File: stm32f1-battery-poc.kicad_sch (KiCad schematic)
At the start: 0 parts

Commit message: schem: add STM32F103C8T6 symbol
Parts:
- added U1: STM32F103C8Tx, Package_QFP:LQFP-48_7x7mm_P0.5mm, symbol MCU_ST_STM32F1:STM32F103C8Tx
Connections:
- new net GND: U1.23 (VSS), U1.35 (VSS), U1.47 (VSS), U1.8 (VSSA)

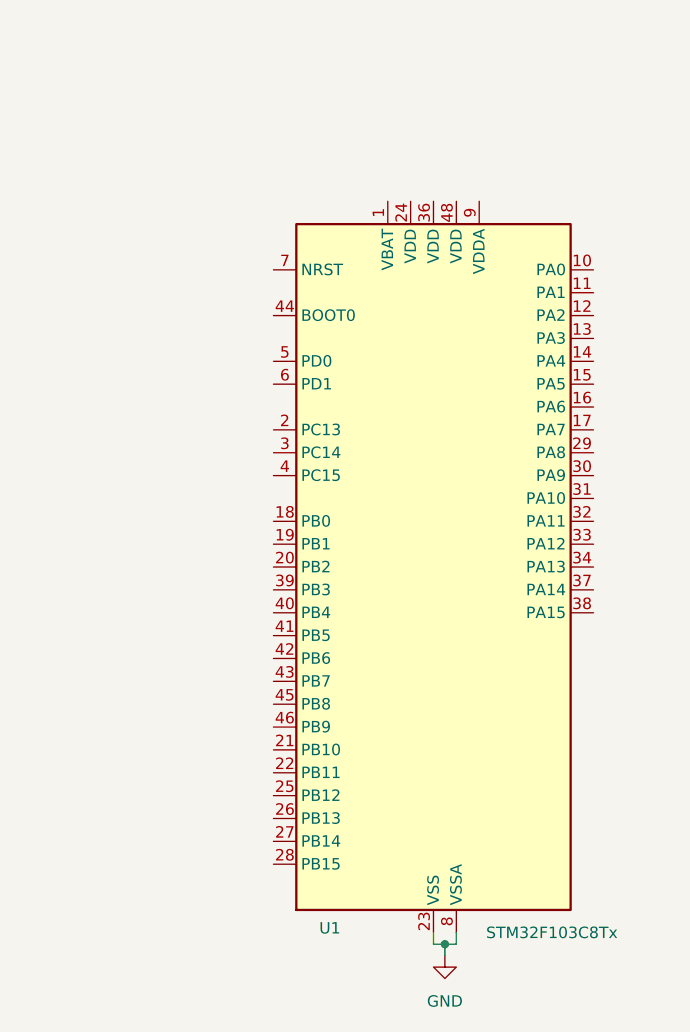
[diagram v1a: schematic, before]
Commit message: schem: add decoupling capacitors
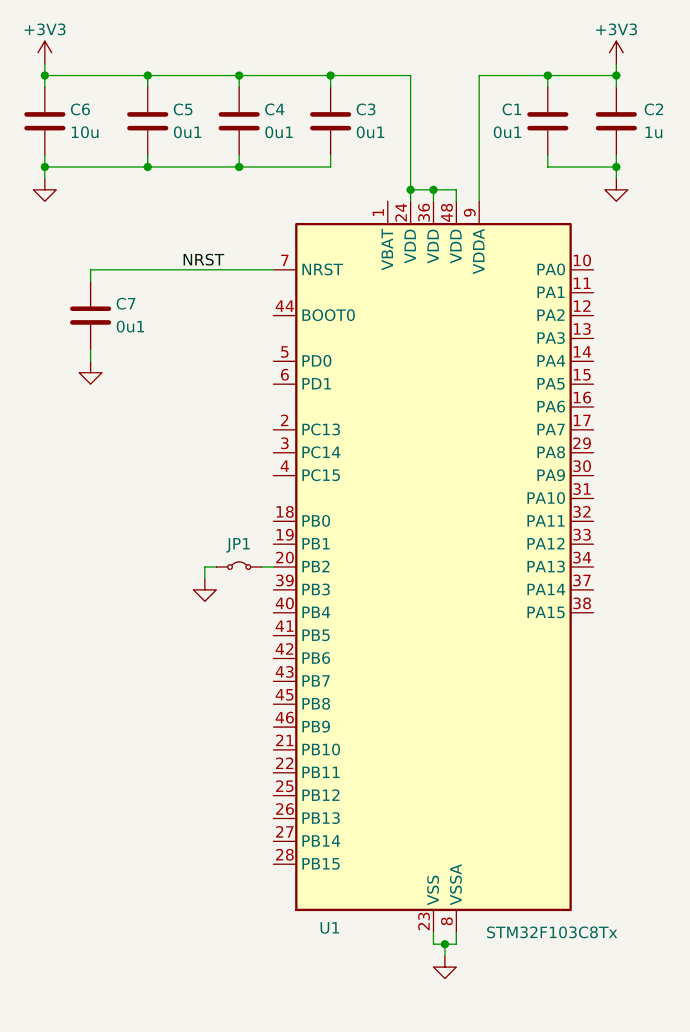
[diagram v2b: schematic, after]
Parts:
- added C1, C3, C4, C5, C7: 0u1, symbol Device:C
- added C2: 1u, symbol Device:C
- added C6: 10u, symbol Device:C
- added JP1: Jumper_2_Small_Bridged, symbol Jumper:Jumper_2_Small_Bridged
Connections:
- net GND: now also C1.2, C2.2, C3.2, C4.2, C5.2, C6.2, C7.2, JP1.1 (A)
- net at U1.20 (PB2): now also JP1.2 (B)
- net +3V3: now reaches U1.24 (VDD)
- net +3V3: now also U1.36 (VDD), U1.48 (VDD), U1.9 (VDDA), C1.1, C2.1, C3.1, C4.1, C5.1, C6.1
- net NRST: now reaches U1.7 (NRST)
- net NRST: now also C7.1

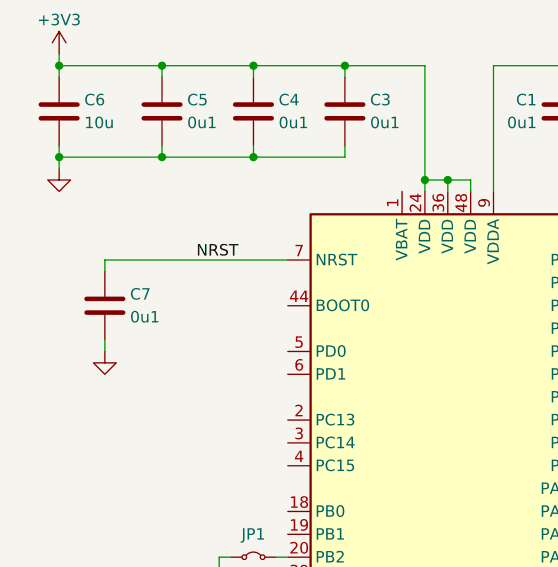
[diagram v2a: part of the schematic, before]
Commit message: schem: add BOOT0 pulldown
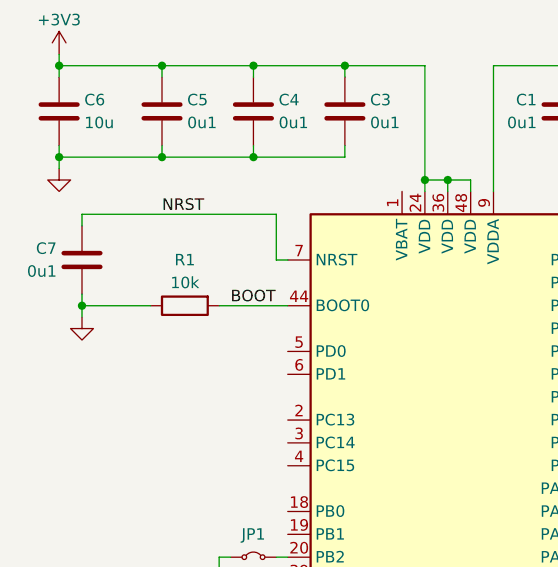
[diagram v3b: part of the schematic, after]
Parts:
- added R1: 10k, symbol Device:R
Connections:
- net GND: now also R1.1
- net BOOT: now reaches U1.44 (BOOT0)
- net BOOT: now also R1.2
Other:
- moved on the sheet: C7
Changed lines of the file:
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@@
+	)
+	(junction
+		(at 110.49 62.23)
+		(diameter 0)
+		(color 0 0 0 0)
 	)
 	(junction
@@
 	(wire
 		(pts
+			(xy 132.08 57.15) (xy 133.35 57.15)
+		)
+		(stroke
+			(width 0)
+			(type default)
+		)
+	)
+	(wire
+		(pts
 			(xy 107.95 45.72) (xy 107.95 44.45)
 		)
@@
 	(wire
 		(pts
+			(xy 110.49 62.23) (xy 118.11 62.23)
+		)
+		(stroke
+			(width 0)
+			(type default)
+		)
+	)
+	(wire
+		(pts
 			(xy 153.67 48.26) (xy 151.13 48.26)
 		)
@@
 	(wire
 		(pts
-			(xy 113.03 66.04) (xy 113.03 67.31)
+			(xy 110.49 60.96) (xy 110.49 62.23)
 		)
 		(stroke
@@
 	(wire
 		(pts
-			(xy 113.03 57.15) (xy 133.35 57.15)
+			(xy 110.49 52.07) (xy 132.08 52.07)
+		)
+		(stroke
+			(width 0)
+			(type default)
+		)
+	)
+	(wire
+		(pts
+			(xy 110.49 62.23) (xy 110.49 63.5)
 		)
 		(stroke
@@
 	(wire
 		(pts
-			(xy 113.03 57.15) (xy 113.03 58.42)
+			(xy 110.49 52.07) (xy 110.49 53.34)
 		)
 		(stroke
@@
 	(wire
 		(pts
+			(xy 125.73 62.23) (xy 133.35 62.23)
+		)
+		(stroke
+			(width 0)
+			(type default)
+		)
+	)
+	(wire
+		(pts
 			(xy 171.45 34.29) (xy 171.45 35.56)
 		)
@@
 	(wire
 		(pts
+			(xy 132.08 52.07) (xy 132.08 57.15)
+		)
+		(stroke
+			(width 0)
+			(type default)
+		)
+	)
+	(wire
+		(pts
 			(xy 163.83 44.45) (xy 163.83 45.72)
 		)
@@
 		)
 	)
+	(label "BOOT"
+		(at 127 62.23 0)
+		(effects
+			(font
+				(size 1.27 1.27)
+			)
+			(justify left bottom)
+		)
+	)
 	(label "NRST"
-		(at 123.19 57.15 0)
+		(at 119.38 52.07 0)
 		(effects
 			(font
@@
 				(path "/4c4b6aca-9f6a-4aac-860b-eb4aeeeecc92"
 					(reference "U1")
+					(unit 1)
+				)
+			)
+		)
+	)
+	(symbol
+		(lib_id "Device:R")
+		(at 121.92 62.23 90)
+		(mirror x)
+		(unit 1)
+		(exclude_from_sim no)
+		(in_bom yes)
+		(on_board yes)
+		(dnp no)
+		(property "Reference" "R1"
+			(at 121.92 57.15 90)
+			(effects
+				(font
+					(size 1.27 1.27)
+				)
+			)
+		)
+		(property "Value" "10k"
+			(at 121.92 59.69 90)
+			(effects
+				(font
+					(size 1.27 1.27)
+				)
+			)
+		)
+		(property "Footprint" ""
+			(at 121.92 60.452 90)
+			(effects
+				(font
+					(size 1.27 1.27)
+				)
+				(hide yes)
+			)
+		)
+		(property "Datasheet" "~"
+			(at 121.92 62.23 0)
+			(effects
+				(font
+					(size 1.27 1.27)
+				)
+				(hide yes)
+			)
+		)
+		(property "Description" "Resistor"
+			(at 121.92 62.23 0)
+			(effects
+				(font
+					(size 1.27 1.27)
+				)
+				(hide yes)
+			)
+		)
+		(pin "2"
+		)
+		(pin "1"
+		)
+		(instances
+			(project ""
+				(path "/4c4b6aca-9f6a-4aac-860b-eb4aeeeecc92"
+					(reference "R1")
 					(unit 1)
 				)
@@
 	(symbol
 		(lib_id "Device:C")
-		(at 113.03 62.23 0)
+		(at 110.49 57.15 0)
+		(mirror y)
 		(unit 1)
 		(exclude_from_sim no)
@@
 		(dnp no)
 		(property "Reference" "C7"
-			(at 115.824 60.96 0)
+			(at 107.696 55.88 0)
 			(effects
 				(font
@@
 		)
 		(property "Value" "0u1"
-			(at 115.824 63.5 0)
+			(at 107.696 58.42 0)
 			(effects
 				(font
@@
 		)
 		(property "Footprint" ""
-			(at 113.9952 66.04 0)
+			(at 109.5248 60.96 0)
 			(effects
 				(font
@@
 		)
 		(property "Datasheet" "~"
-			(at 113.03 62.23 0)
+			(at 110.49 57.15 0)
 			(effects
 				(font
@@
 		)
 		(property "Description" "Unpolarized capacitor"
-			(at 113.03 62.23 0)
+			(at 110.49 57.15 0)
 			(effects
 				(font
@@
 	(symbol
 		(lib_id "power:GND")
-		(at 113.03 67.31 0)
+		(at 110.49 63.5 0)
 		(unit 1)
 		(exclude_from_sim no)
@@
 		(fields_autoplaced yes)
 		(property "Reference" "#PWR06"
-			(at 113.03 73.66 0)
+			(at 110.49 69.85 0)
 			(effects
 				(font
@@
 		)
 		(property "Value" "GND"
-			(at 113.03 72.39 0)
+			(at 110.49 68.58 0)
 			(effects
 				(font
@@
 		)
 		(property "Footprint" ""
-			(at 113.03 67.31 0)
+			(at 110.49 63.5 0)
 			(effects
 				(font
@@
 		)
 		(property "Datasheet" ""
-			(at 113.03 67.31 0)
+			(at 110.49 63.5 0)
 			(effects
 				(font
@@
 		)
 		(property "Description" "Power symbol creates a global label with name \"GND\" , ground"
-			(at 113.03 67.31 0)
-			(effects
-				(font
+			(at 110.49 63.5 0)
+			(effects
+				(font

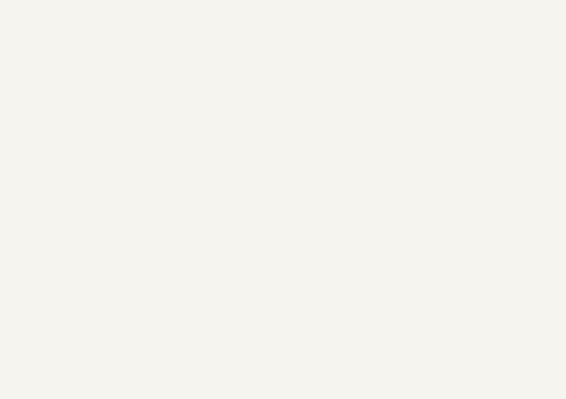
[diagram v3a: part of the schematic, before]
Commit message: pcb: add BOOT and RST buttons
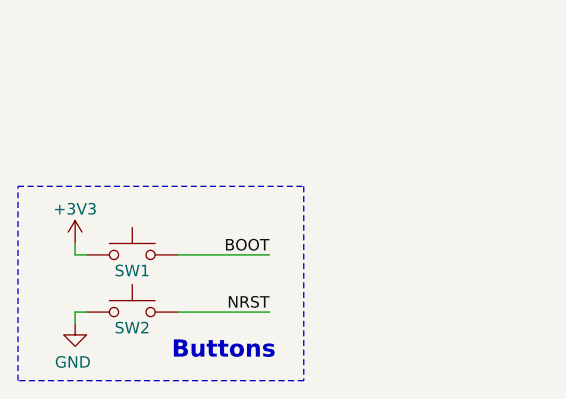
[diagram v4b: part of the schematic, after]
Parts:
- added SW1, SW2: SW_Push, Button_Switch_SMD:SW_SPST_TS-1088-xR020, symbol Switch:SW_Push
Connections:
- net +3V3: now also SW1.1
- net BOOT: now also SW1.2
- net GND: now also SW2.1
- net NRST: now also SW2.2
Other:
- note added: "Buttons"

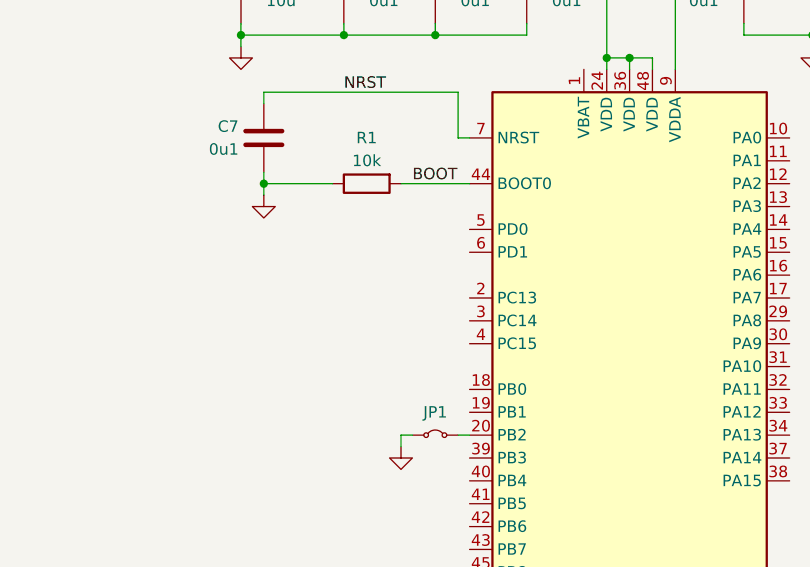
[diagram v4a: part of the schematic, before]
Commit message: schem: add 8Mhz HSE
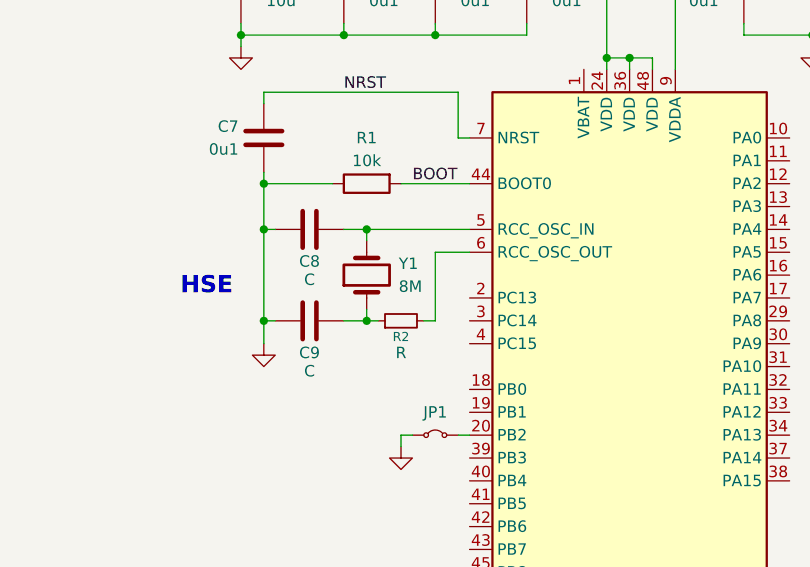
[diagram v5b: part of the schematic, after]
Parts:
- added C8, C9: C, symbol Device:C
- added R2: R, symbol Device:R_Small
- added Y1: 8M, symbol Device:Crystal
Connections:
- net GND: now also C8.2, C9.2
- net at U1.5 (PD0): now also C8.1, Y1.2
- net at U1.6 (PD1): now also R2.2
- new net: C9.1, R2.1, Y1.1
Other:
- note added: "HSE"

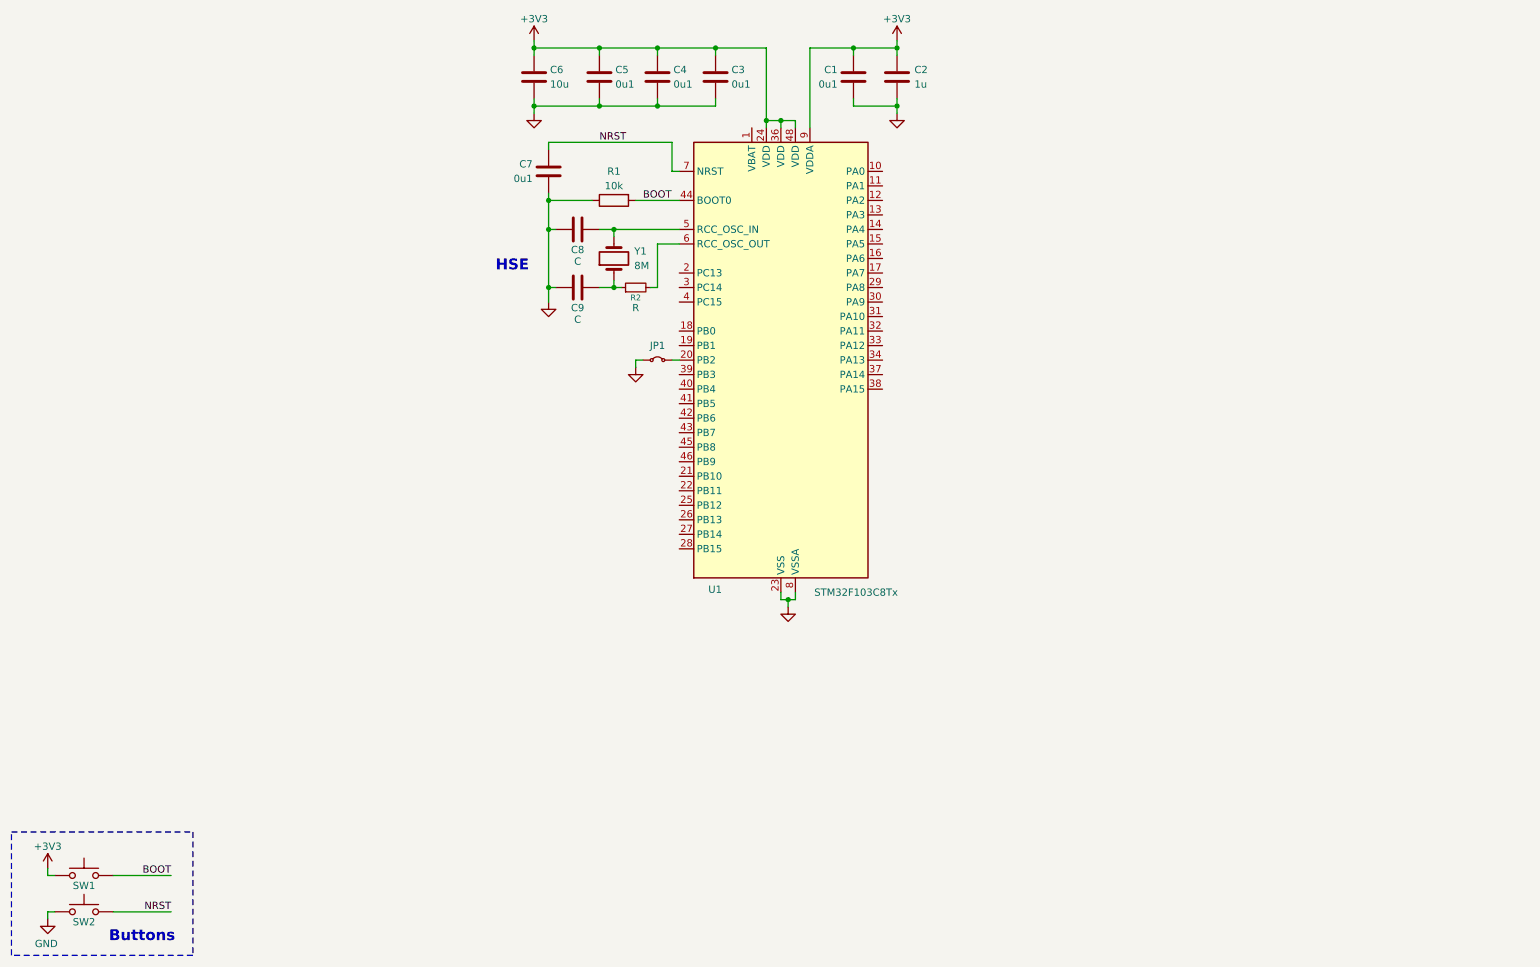
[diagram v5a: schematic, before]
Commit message: schem: add STDC14 Debug port
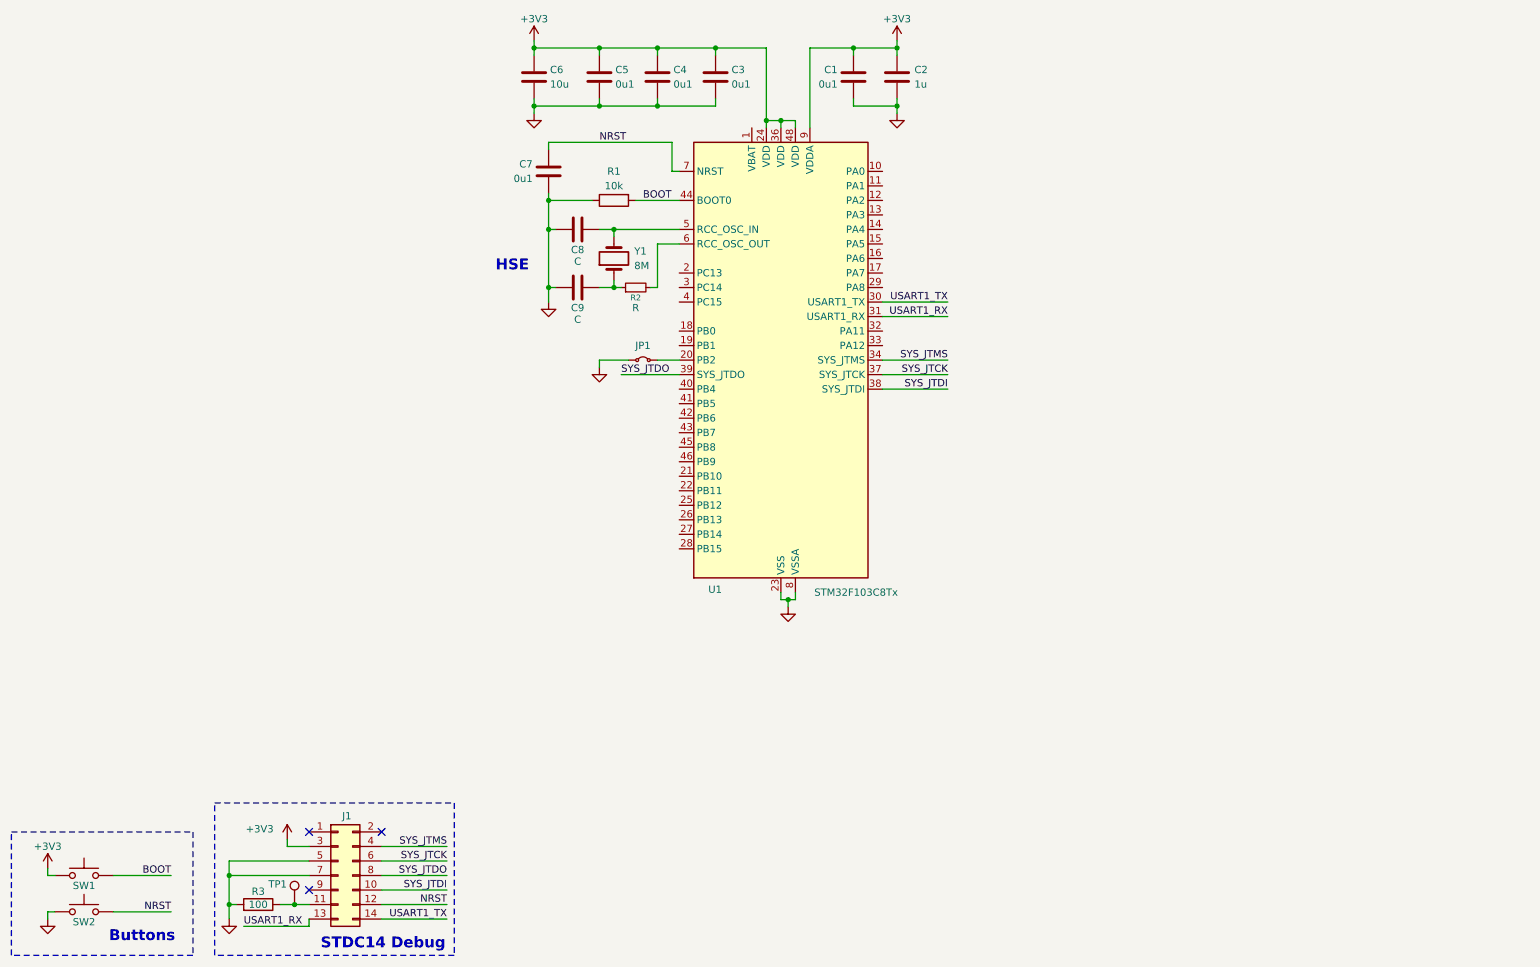
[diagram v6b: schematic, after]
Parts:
- added J1: Conn_02x07_Odd_Even, symbol Connector_Generic:Conn_02x07_Odd_Even
- added R3: 100, symbol Device:R
- added TP1: TestPoint, symbol Connector:TestPoint
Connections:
- net +3V3: now also J1.3 (Pin_3)
- net GND: now also J1.5 (Pin_5), J1.7 (Pin_7), R3.2
- net NRST: now also J1.12 (Pin_12)
- net USART1_TX: now reaches U1.30 (PA9)
- net USART1_TX: now also J1.14 (Pin_14)
- net USART1_RX: now reaches U1.31 (PA10)
- net USART1_RX: now also J1.13 (Pin_13)
- net SYS_JTMS: now reaches U1.34 (PA13)
- net SYS_JTMS: now also J1.4 (Pin_4)
- net SYS_JTCK: now reaches U1.37 (PA14)
- net SYS_JTCK: now also J1.6 (Pin_6)
- net SYS_JTDI: now reaches U1.38 (PA15)
- net SYS_JTDI: now also J1.10 (Pin_10)
- net SYS_JTDO: now reaches U1.39 (PB3)
- net SYS_JTDO: now also J1.8 (Pin_8)
- new net: J1.11 (Pin_11), R3.1, TP1.1
- no-connect marks 0 -> 3
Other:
- note added: "STDC14 Debug"
- moved on the sheet: JP1
